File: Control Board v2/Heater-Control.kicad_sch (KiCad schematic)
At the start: 0 parts

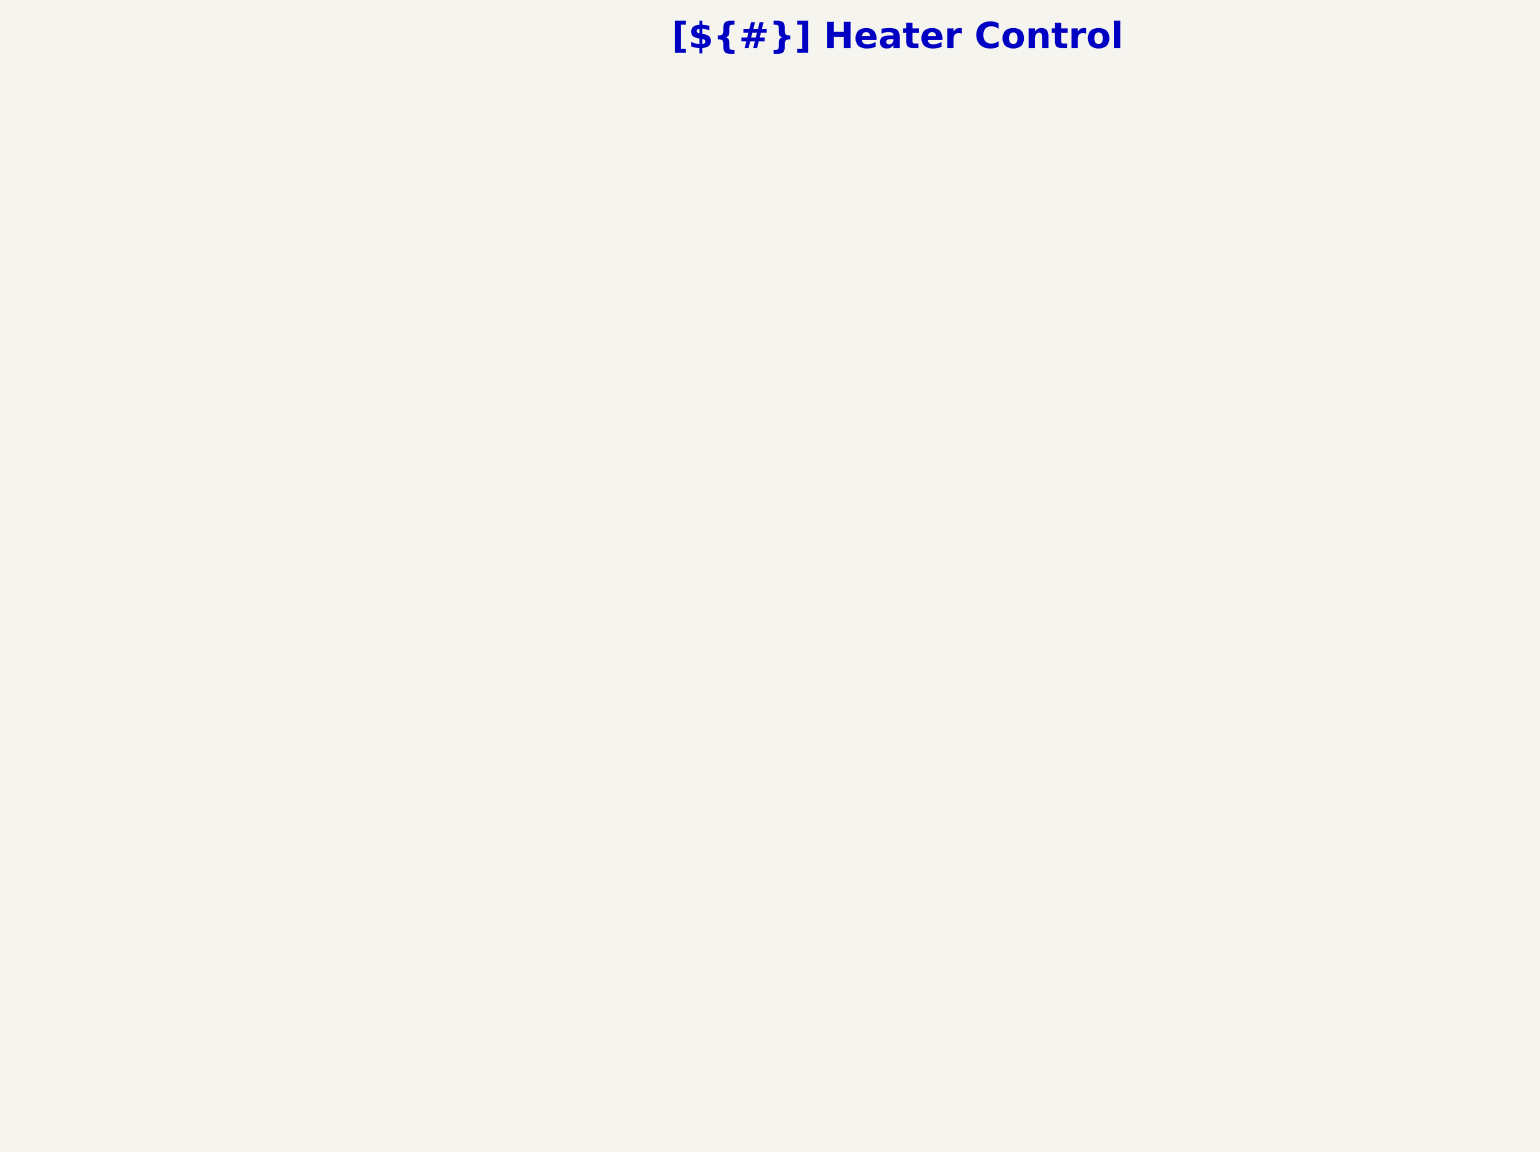
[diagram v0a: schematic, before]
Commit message: Draft power supply and TRIAC driver circuits
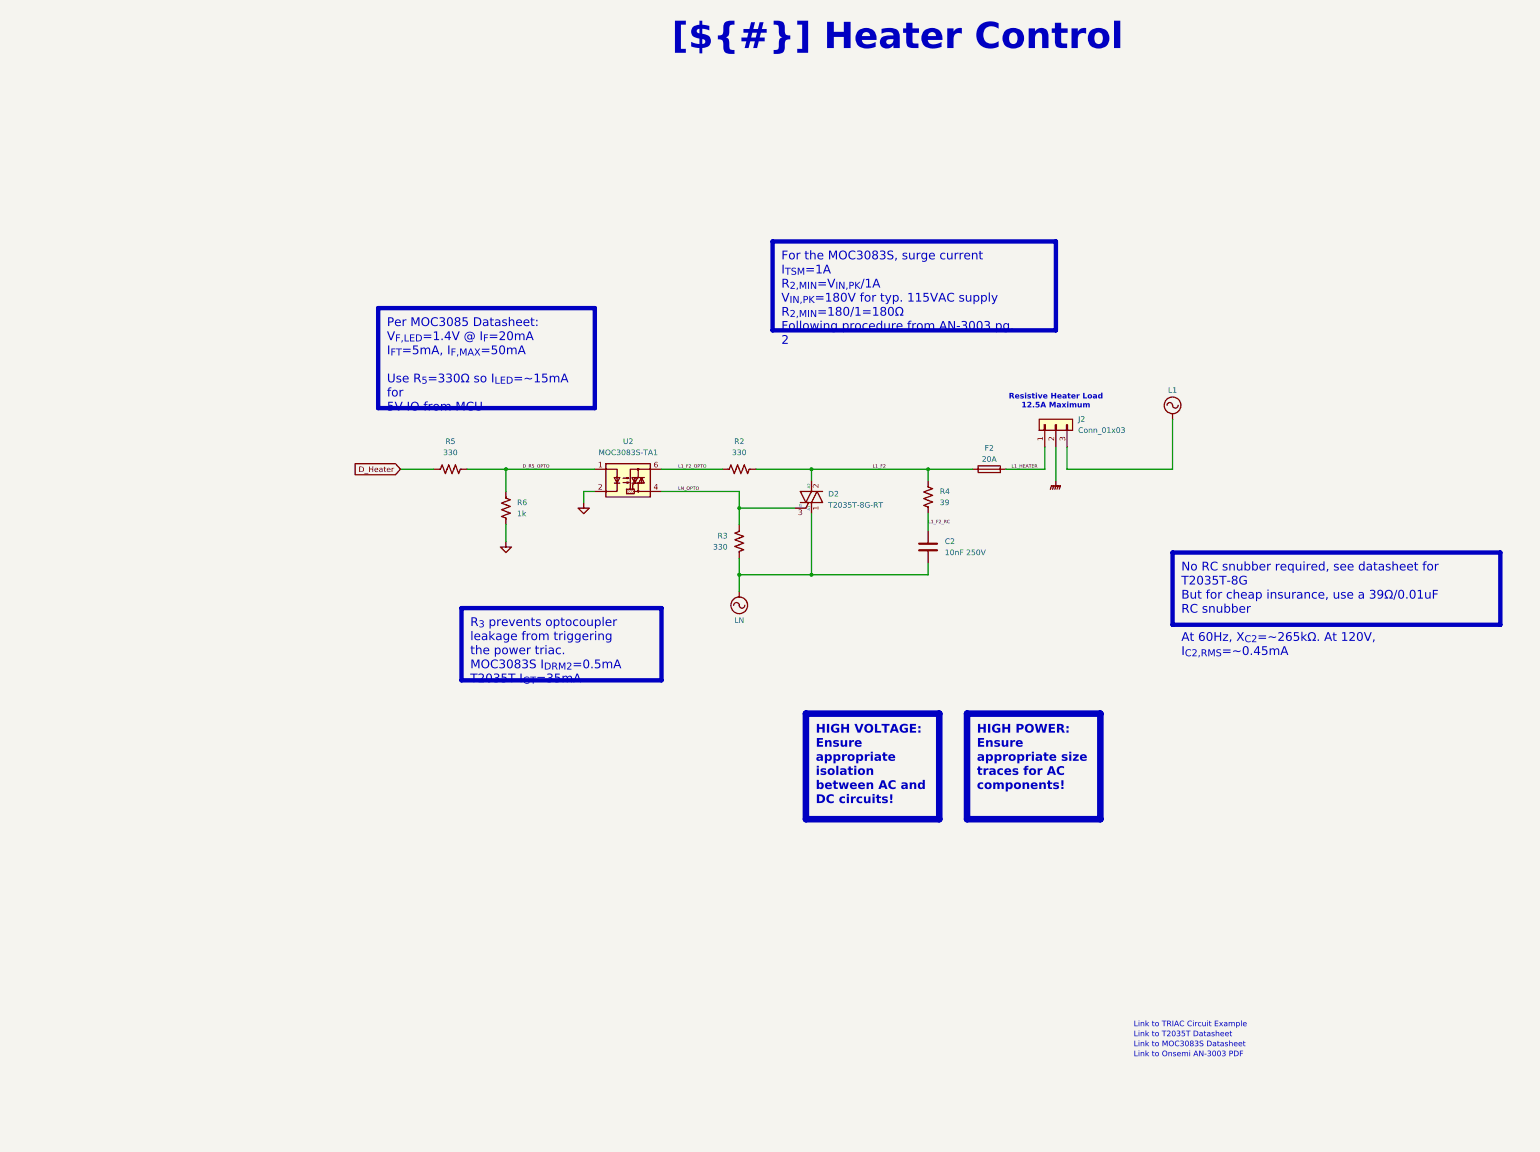
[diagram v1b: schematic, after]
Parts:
- added C2: 10nF 250V, symbol Device:C
- added D2: T2035T-8G-RT, symbol Triac_Thyristor:Generic_Triac_A1A2G
- added F2: 20A, symbol Device:Fuse
- added J2: Conn_01x03, symbol Connector_Generic:Conn_01x03
- added R2, R3, R5: 330, symbol Device:R_US
- added R4: 39, symbol Device:R_US
- added R6: 1k, symbol Device:R_US
- added U2: MOC3083S-TA1, symbol Relay_SolidState:MOC3083M
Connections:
- new net D_Heater: R5.1
- new net D_R5_OPTO: R5.2, R6.2, U2.1
- new net GND: R6.1, U2.2
- new net GNDPWR: J2.2 (Pin_2)
- new net L1: J2.3 (Pin_3)
- new net L1_F2: D2.2 (A2), F2.1, R2.2, R4.2
- new net L1_F2_OPTO: R2.1, U2.6
- new net L1_F2_RC: C2.1, R4.1
- new net L1_HEATER: F2.2, J2.1 (Pin_1)
- new net LN: C2.2, D2.1 (A1), R3.1
- new net LN_OPTO: D2.3 (G), R3.2, U2.4
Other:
- note added: "Link to MOC3083S Datasheet"
- note added: "Link to Onsemi AN-3003 PDF"
- note added: "Link to T2035T Datasheet"
- note added: "Link to TRIAC Circuit Example"
- note added: "Resistive Heater Load 12.5A Maximum"

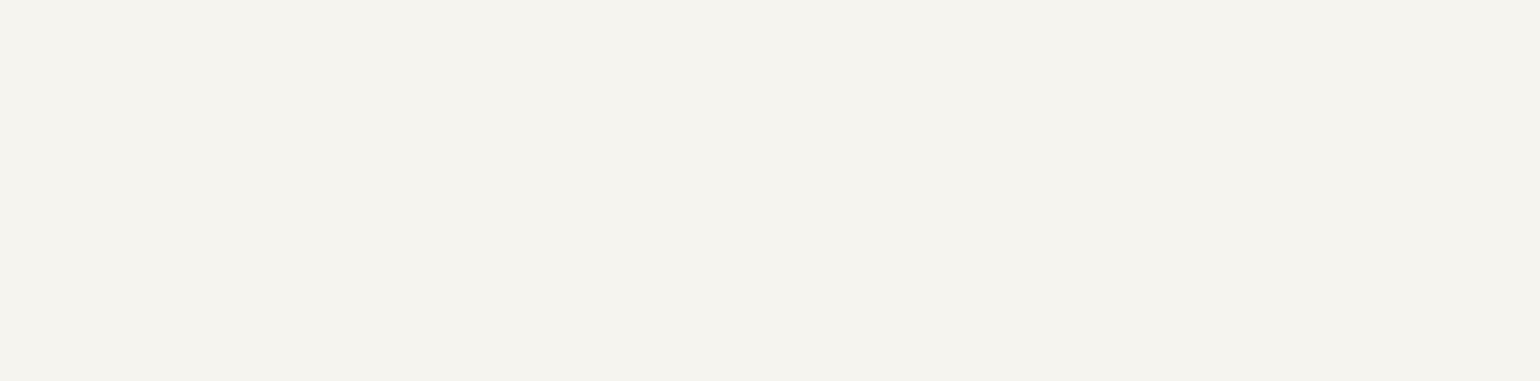
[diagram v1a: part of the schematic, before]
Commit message: add resource links
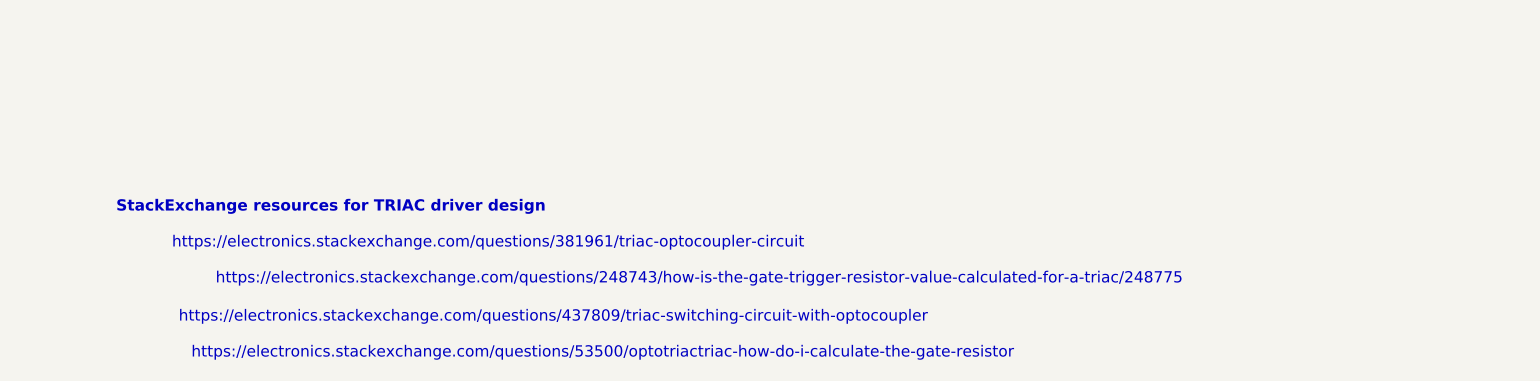
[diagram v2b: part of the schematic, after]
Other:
- note added: "StackExchange resources for TRIAC driver design"
- note added: "https://electronics.stackexchange.com/questions/248743/how-is-the-gate-trigger-resistor-value-calculated-for-a-triac/248775"
- note added: "https://electronics.stackexchange.com/questions/381961/triac-optocoupler-circuit"
- note added: "https://electronics.stackexchange.com/questions/437809/triac-switching-circuit-with-optocoupler"
- note added: "https://electronics.stackexchange.com/questions/53500/optotriactriac-how-do-i-calculate-the-gate-resistor"
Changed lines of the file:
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@@
+		)
+	)
+	(text "https://electronics.stackexchange.com/questions/381961/triac-optocoupler-circuit"
+		(exclude_from_sim no)
+		(at 60.198 261.112 0)
+		(effects
+			(font
+				(size 1.27 1.27)
+			)
+		)
+	)
+	(text "StackExchange resources for TRIAC driver design"
+		(exclude_from_sim no)
+		(at 42.418 257.048 0)
+		(effects
+			(font
+				(size 1.27 1.27)
+				(thickness 0.254)
+				(bold yes)
+			)
+		)
+	)
+	(text "https://electronics.stackexchange.com/questions/53500/optotriactriac-how-do-i-calculate-the-gate-resistor"
+		(exclude_from_sim no)
+		(at 73.152 273.558 0)
+		(effects
+			(font
+				(size 1.27 1.27)
+			)
 		)
 	)
@@
 			)
 		)
+	)
+	(text "https://electronics.stackexchange.com/questions/248743/how-is-the-gate-trigger-resistor-value-calculated-for-a-triac/248775"
+		(exclude_from_sim no)
+		(at 84.074 265.176 0)
+		(effects
+			(font
+				(size 1.27 1.27)
+			)
+		)
+	)
+	(text "https://electronics.stackexchange.com/questions/437809/triac-switching-circuit-with-optocoupler"
+		(exclude_from_sim no)
+		(at 67.564 269.494 0)
+		(effects
+			(font
+				(size 1.27 1.27)
+			)
+		)

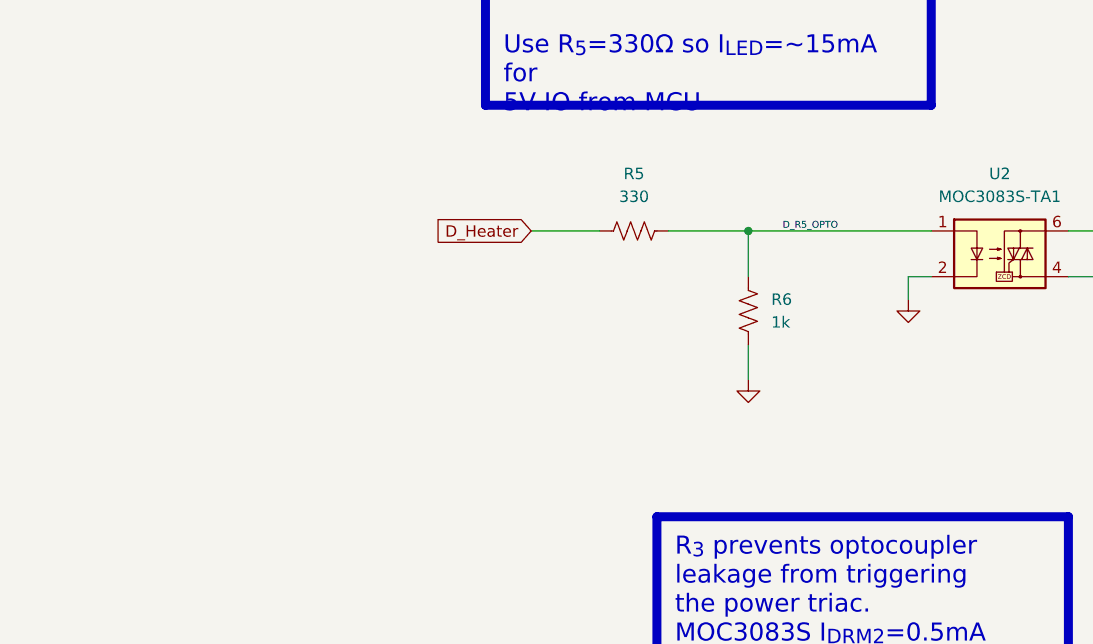
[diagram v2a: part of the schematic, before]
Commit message: draft microcontroller and interface circuits, still need to finish interfaces
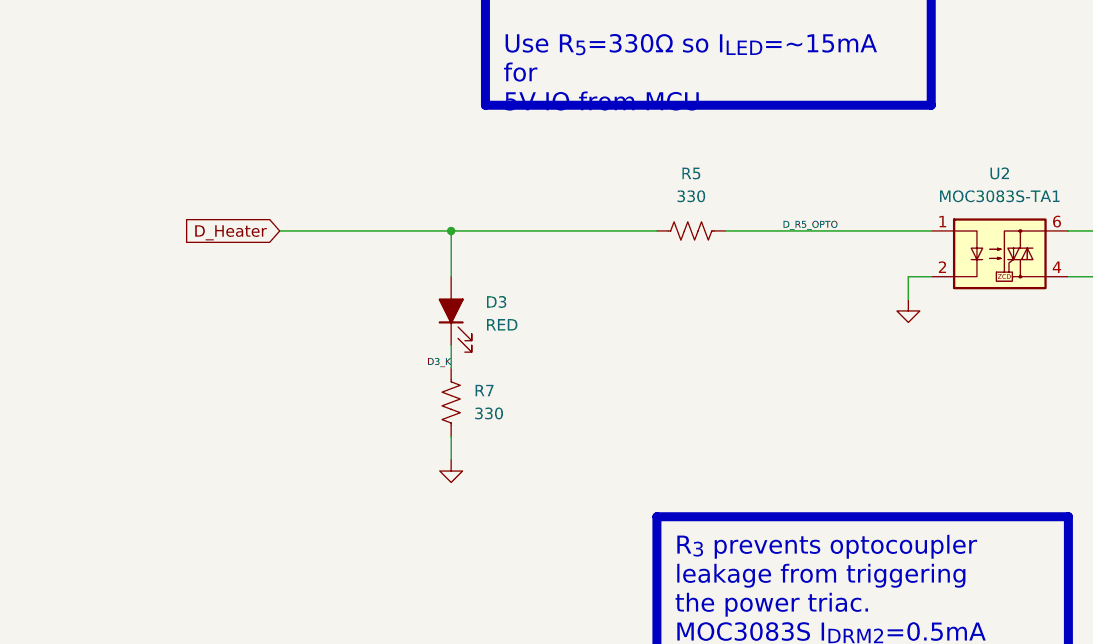
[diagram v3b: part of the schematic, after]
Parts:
- removed R6: 1k, symbol Device:R_US
- added D3: RED, symbol Device:LED_Filled
- added R7: 330, symbol Device:R_US
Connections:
- net D_Heater: now also D3.2 (A)
- net GND: now also R7.2
- new net D3_K: D3.1 (K), R7.1
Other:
- moved on the sheet: R5

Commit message: work on PCB layout
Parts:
- C2: footprint (none) -> Capacitor_SMD:C_1206_3216Metric_Pad1.33x1.80mm_HandSolder
- D2: footprint (none) -> Package_TO_SOT_SMD:TO-263-2
- D3: footprint (none) -> LED_SMD:LED_0603_1608Metric_Pad1.05x0.95mm_HandSolder
- F2: footprint (none) -> Fuse:Fuse_Blade_ATO_directSolder
- J2: value Conn_01x03 -> 1366005; footprint (none) -> PhoenixContact_SPTA:SPTA-THR 2.53-5.0 P26
- R2, R3, R4: footprint (none) -> Resistor_SMD:R_2512_6332Metric_Pad1.40x3.35mm_HandSolder
- R5, R7: footprint (none) -> Resistor_SMD:R_0603_1608Metric_Pad0.98x0.95mm_HandSolder
- U2: footprint (none) -> Package_DIP:SMDIP-6_W9.53mm
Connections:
- net L1: now also J2.1 (Pin_1); no longer J2.3 (Pin_3)
- net L1_HEATER: now also J2.3 (Pin_3); no longer J2.1 (Pin_1)
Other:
- moved on the sheet: D3, J2, R7
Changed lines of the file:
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@@
 	(wire
 		(pts
-			(xy 87.63 125.73) (xy 87.63 120.65)
+			(xy 87.63 124.46) (xy 87.63 120.65)
 		)
 		(stroke
@@
 	(wire
 		(pts
-			(xy 87.63 133.35) (xy 87.63 135.89)
+			(xy 87.63 132.08) (xy 87.63 134.62)
 		)
 		(stroke
@@
 	(wire
 		(pts
-			(xy 87.63 143.51) (xy 87.63 146.05)
+			(xy 87.63 142.24) (xy 87.63 144.78)
 		)
 		(stroke
@@
 	)
 	(label "D3_K"
-		(at 87.63 135.89 180)
+		(at 87.63 134.62 180)
 		(effects
 			(font
@@
 			)
 		)
-		(property "Footprint" ""
+		(property "Footprint" "Resistor_SMD:R_2512_6332Metric_Pad1.40x3.35mm_HandSolder"
 			(at 175.006 136.906 90)
 			(effects
@@
 			)
 		)
-		(property "Footprint" ""
+		(property "Footprint" "Capacitor_SMD:C_1206_3216Metric_Pad1.33x1.80mm_HandSolder"
 			(at 218.1352 142.24 0)
 			(effects
@@
 			)
 		)
-		(property "Footprint" ""
+		(property "Footprint" "Resistor_SMD:R_2512_6332Metric_Pad1.40x3.35mm_HandSolder"
 			(at 216.154 126.746 90)
 			(effects
@@
 	(symbol
 		(lib_id "Connector_Generic:Conn_01x03")
-		(at 246.38 110.49 90)
-		(unit 1)
-		(exclude_from_sim no)
-		(in_bom yes)
-		(on_board yes)
-		(dnp no)
-		(fields_autoplaced yes)
+		(at 246.38 110.49 270)
+		(mirror x)
+		(unit 1)
+		(exclude_from_sim no)
+		(in_bom yes)
+		(on_board yes)
+		(dnp no)
 		(property "Reference" "J2"
-			(at 251.46 109.2199 90)
+			(at 241.3 109.2199 90)
 			(effects
 				(font
@@
 			)
 		)
-		(property "Value" "Conn_01x03"
-			(at 251.46 111.7599 90)
+		(property "Value" "1366005"
+			(at 241.3 111.7599 90)
 			(effects
 				(font
@@
 			)
 		)
-		(property "Footprint" ""
+		(property "Footprint" "PhoenixContact_SPTA:SPTA-THR 2.53-5.0 P26"
 			(at 246.38 110.49 0)
 			(effects
@@
 	(symbol
 		(lib_id "Device:R_US")
-		(at 87.63 139.7 0)
+		(at 87.63 138.43 0)
 		(unit 1)
 		(exclude_from_sim no)
@@
 		(fields_autoplaced yes)
 		(property "Reference" "R7"
-			(at 90.17 138.4299 0)
+			(at 90.17 137.1599 0)
 			(effects
 				(font
@@
 		)
 		(property "Value" "330"
-			(at 90.17 140.9699 0)
+			(at 90.17 139.6999 0)
 			(effects
 				(font
@@
 			)
 		)
-		(property "Footprint" ""
-			(at 88.646 139.954 90)
+		(property "Footprint" "Resistor_SMD:R_0603_1608Metric_Pad0.98x0.95mm_HandSolder"
+			(at 88.646 138.684 90)
 			(effects
 				(font
@@
 		)
 		(property "Datasheet" "~"
-			(at 87.63 139.7 0)
+			(at 87.63 138.43 0)
 			(effects
 				(font
@@
 		)
 		(property "Description" "Resistor, US symbol"
-			(at 87.63 139.7 0)
+			(at 87.63 138.43 0)
 			(effects
 				(font
@@
 			)
 		)
-		(property "Footprint" ""
+		(property "Footprint" "Package_TO_SOT_SMD:TO-263-2"
 			(at 192.405 126.365 90)
 			(effects
@@
 	(symbol
 		(lib_id "power:GND")
-		(at 87.63 146.05 0)
+		(at 87.63 144.78 0)
 		(unit 1)
 		(exclude_from_sim no)
@@
 		(fields_autoplaced yes)
 		(property "Reference" "#PWR018"
-			(at 87.63 152.4 0)
+			(at 87.63 151.13 0)
 			(effects
 				(font
@@
 		)
 		(property "Value" "GND"
-			(at 87.63 151.13 0)
+			(at 87.63 149.86 0)
 			(effects
 				(font
@@
 		)
 		(property "Footprint" ""
-			(at 87.63 146.05 0)
+			(at 87.63 144.78 0)
 			(effects
 				(font
@@
 		)
 		(property "Datasheet" ""
-			(at 87.63 146.05 0)
+			(at 87.63 144.78 0)
 			(effects
 				(font
@@
 		)
 		(property "Description" "Power symbol creates a global label with name \"GND\" , ground"
-			(at 87.63 146.05 0)
+			(at 87.63 144.78 0)
 			(effects
 				(font
@@
 			)
 		)
-		(property "Footprint" ""
+		(property "Footprint" "Resistor_SMD:R_0603_1608Metric_Pad0.98x0.95mm_HandSolder"
 			(at 114.554 119.634 90)
 			(effects
@@
 	(symbol
 		(lib_id "Device:LED_Filled")
-		(at 87.63 129.54 90)
+		(at 87.63 128.27 90)
 		(unit 1)
 		(exclude_from_sim no)
@@
 		(fields_autoplaced yes)
 		(property "Reference" "D3"
-			(at 91.44 128.5874 90)
+			(at 91.44 127.3174 90)
 			(effects
 				(font
@@
 		)
 		(property "Value" "RED"
-			(at 91.44 131.1274 90)
+			(at 91.44 129.8574 90)
 			(effects
 				(font
@@
 			)
 		)
-		(property "Footprint" ""
-			(at 87.63 129.54 0)
+		(property "Footprint" "LED_SMD:LED_0603_1608Metric_Pad1.05x0.95mm_HandSolder"
+			(at 87.63 128.27 0)
 			(effects
 				(font
@@
 		)
 		(property "Datasheet" "~"
-			(at 87.63 129.54 0)
+			(at 87.63 128.27 0)
 			(effects
 				(font
@@
 		)
 		(property "Description" "Light emitting diode, filled shape"
-			(at 87.63 129.54 0)
+			(at 87.63 128.27 0)
 			(effects
 				(font
@@
 			)
 		)
-		(property "Footprint" ""
+		(property "Footprint" "Fuse:Fuse_Blade_ATO_directSolder"
 			(at 231.14 122.428 90)
 			(effects
@@
 			)
 		)
-		(property "Footprint" ""
+		(property "Footprint" "Resistor_SMD:R_2512_6332Metric_Pad1.40x3.35mm_HandSolder"
 			(at 174.244 119.634 90)
 			(effects
@@
 			)
 		)
-		(property "Footprint" ""
+		(property "Footprint" "Package_DIP:SMDIP-6_W9.53mm"
 			(at 143.51 128.27 0)
 			(effects
